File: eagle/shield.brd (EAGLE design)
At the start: 100 x 55.5 mm, 41 parts, among them IC1 ATMEGA328P-AU, J1 22-27-2021-02, Q2 BSS138, Q3 BSS138, T1 BC517

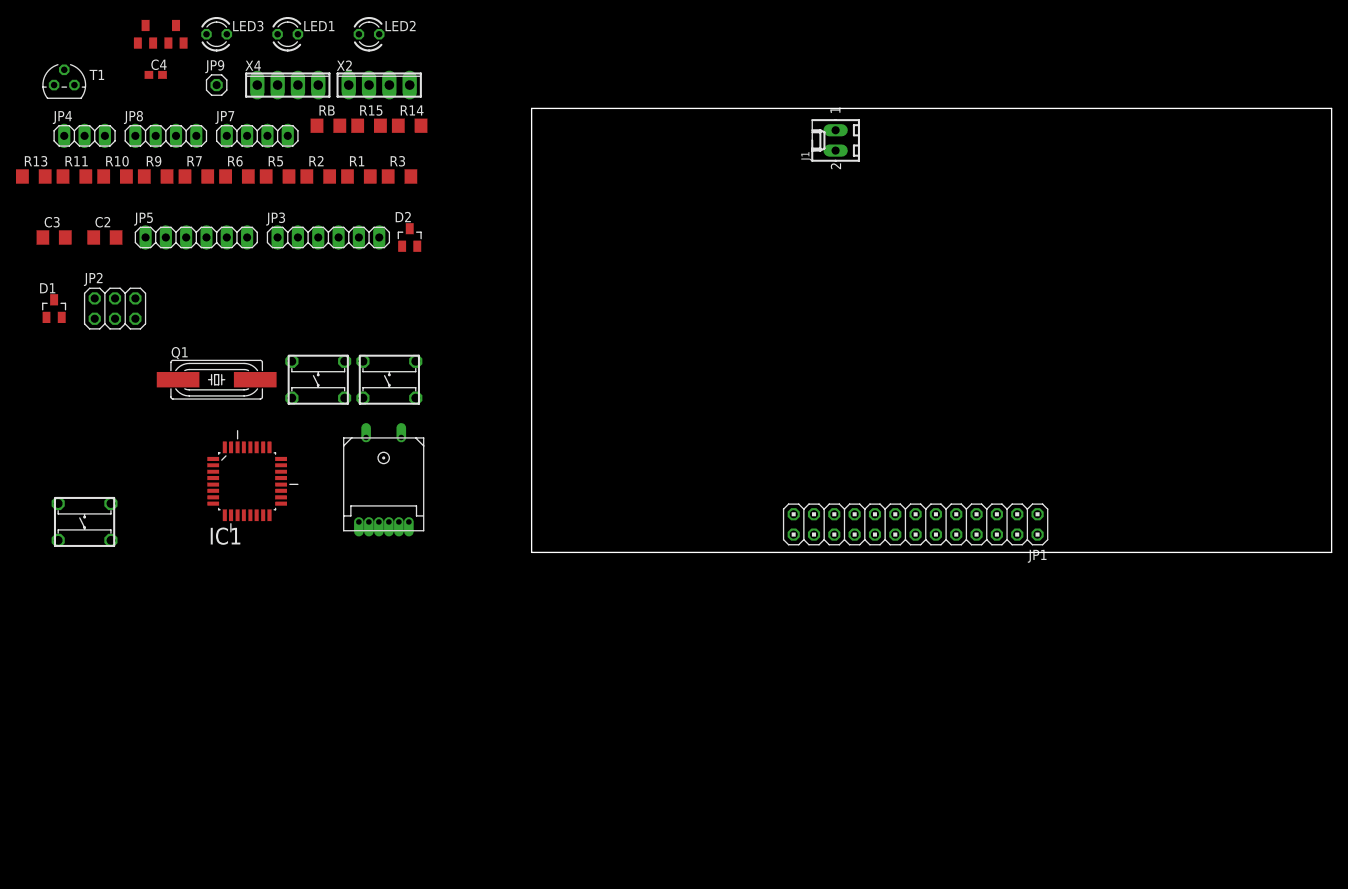
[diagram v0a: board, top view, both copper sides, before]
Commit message: added breakout for navi on an extra board
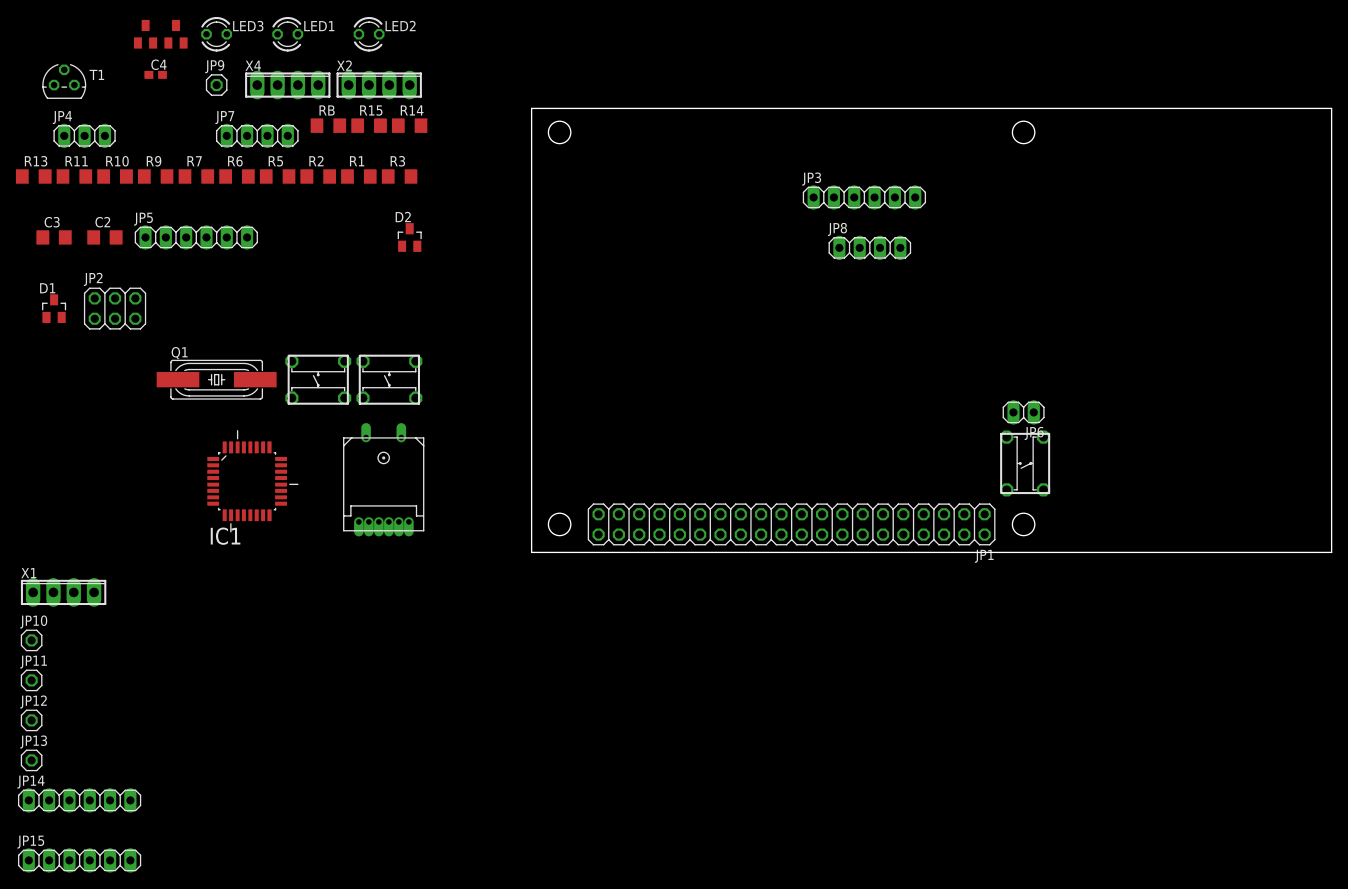
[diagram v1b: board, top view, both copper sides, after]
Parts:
- removed J1: 22-27-2021-02, con-molex:6410-02
- added JP10, JP11, JP12, JP13: (no value), pinhead:1X01
- added JP14: GPS, pinhead:1X06
- added JP15: (no value), pinhead:1X06
- added JP6: (no value), pinhead:1X02
- added X1: (no value), con-phoenix-254:4POL254
- JP1: device pinhead:2X13 -> pinhead:2X20
- moved S1 117.8 mm to (61.7, 11.1), turned to 90 degrees
- moved JP8 89.1 mm to (42.3, 38.1)
- moved JP3 67.2 mm to (41.6, 44.4)
- moved JP1 15.5 mm to (32.5, 3.50)
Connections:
- new net N$13: JP10.1, X1.4
- new net N$14: JP11.1, X1.3
- new net N$15: JP12.1, X1.2
- new net N$16: JP13.1, X1.1
- new net N$17: JP15.1, U$2.P$1
- new net N$18: JP15.6, LED3.K, U$2.P$7, U$2.P$8
- net GND: now also JP14.6; no longer LED3.K, U$2.P$7, U$2.P$8
- net N$27: now also JP6.1; no longer J1.1
- net N$28: now also JP6.2; no longer J1.2
- net N$32: now also JP15.5
- net PWR: now also JP14.4, JP15.4
- net RX: now also JP14.3, JP15.3
- net TX: now also JP14.2, JP15.2
- net VCC: now also JP14.1; no longer U$2.P$1

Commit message: first board design
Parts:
- removed R15: 220, resistor:R1206
- removed RB: 0, resistor:R1206
- removed U$2: NAVILOK-NL-631ETTL, 0liver:NAVILOK-NL-631ETTL
- added R4: 10k, resistor:R1206
- JP15: device pinhead:1X06 -> pinhead:1X02
- moved T1 155.2 mm to (90.6, 14.9)
- moved JP4 152.2 mm to (95.5, 36.0), flipped to the bottom, turned to 90 degrees
- moved D1 138.2 mm to (78.0, 42.0), turned to 270 degrees
- moved X4 134.4 mm to (96.0, 13.0), turned to 90 degrees
- moved R7 134.0 mm to (89.5, 21.0)
- moved JP14 128.7 mm to (48.5, 43.5), turned to 180 degrees
- moved R6 127.2 mm to (89.5, 32.0), turned to 180 degrees
- moved R5 122.6 mm to (89.5, 29.0)
- moved JP5 119.9 mm to (76.5, 20.5)
- moved X2 119.8 mm to (96.0, 25.0), turned to 90 degrees
- moved C3 117.7 mm to (58.0, 39.0), turned to 270 degrees
- moved Q3 116.4 mm to (54.5, 10.0)
- moved JP15 116.1 mm to (43.5, 20.5)
- moved R13 115.9 mm to (49.0, 14.5), turned to 270 degrees
- moved R11 112.7 mm to (49.0, 9.00)
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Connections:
- removed net N$18: JP15.6, LED3.K, U$2.P$7, U$2.P$8
- removed net N$32: JP15.5, R15.1, U$2.P$5
- removed net N$33: LED3.A, R15.2
- net GND: now also JP15.2, LED3.K
- net N$12: now also LED3.A, R4.2; no longer JP1.1, Q3.G, R2.2, RB.2
- net N$17: now also JP1.11, R4.1; no longer JP15.1, U$2.P$1
- net N$51: now also JP1.1, Q3.G, R2.2; no longer RB.1
- net PWR: no longer JP15.4, U$2.P$4
- net RX: no longer JP15.3, U$2.P$3
- net TX: no longer JP15.2, U$2.P$2
- net VCC: now also JP15.1
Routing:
- net VCC: track 0.00 -> 195.7 mm
- net GND: track 0.00 -> 161.5 mm
- net N$26: track 0.00 -> 37.7 mm
- net N$47: track 0.00 -> 36.8 mm
- net N$19: track 0.00 -> 26.3 mm
- net N$51: track 0.00 -> 23.1 mm
- net RES: track 0.00 -> 20.9 mm
- net RESET1: track 0.00 -> 19.7 mm
- net N$17: track 0.00 -> 17.9 mm
- net RX: track 0.00 -> 16.2 mm
- net N$3: track 0.00 -> 14.8 mm
- net N$4: track 0.00 -> 12.9 mm
- net N$11: track 0.00 -> 12.5 mm
- net N$25: track 0.00 -> 11.1 mm
- net N$46: track 0.00 -> 9.04 mm
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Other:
- board text added: "h=10"
- board text added: "h=15"
- board text added: "h=20"
- board text added: "h=5"
